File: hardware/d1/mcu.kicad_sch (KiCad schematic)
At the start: 3 parts, among them U2 STM32G0B1VCT6, U3 STM32G0B1KBU6N, X1 X322516MLB4SI

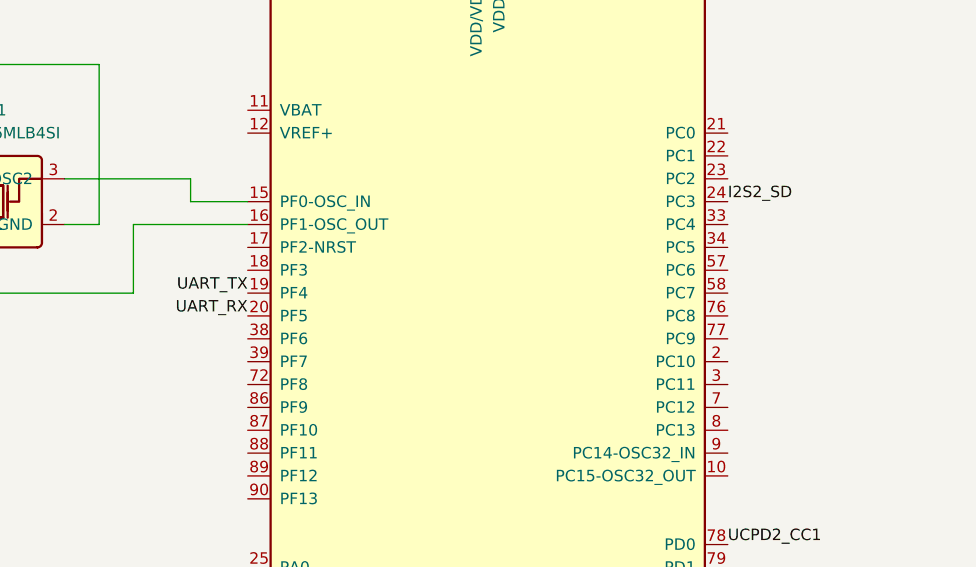
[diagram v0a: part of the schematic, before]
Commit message: Change uart pins, add components
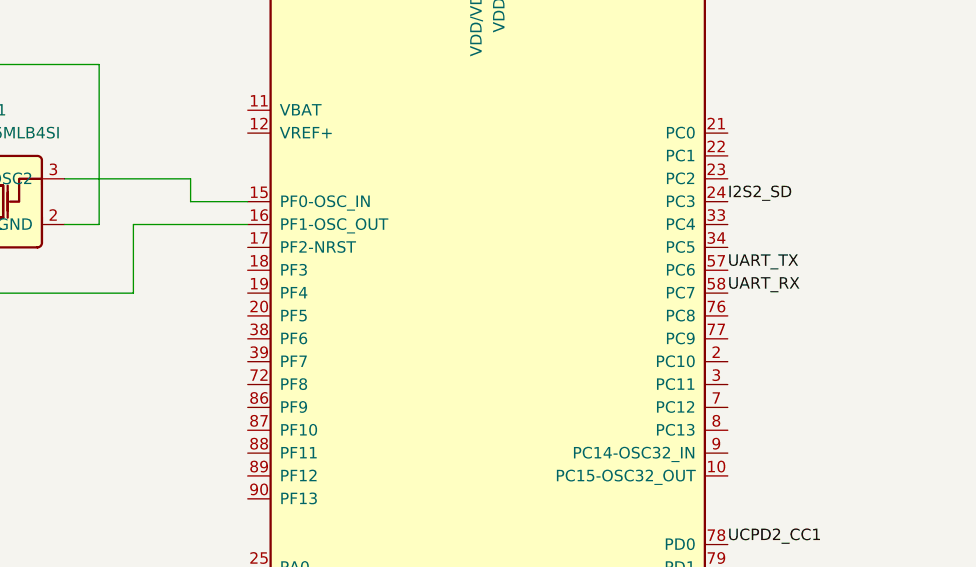
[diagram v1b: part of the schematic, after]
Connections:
- net UART_RX: now also U2.58 (PC7); no longer U2.20 (PF5)
- net UART_TX: now also U2.57 (PC6); no longer U2.19 (PF4)
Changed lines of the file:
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@@
-		)
-	)
-	(label "UART_TX"
-		(at 83.82 58.42 180)
-		(effects
-			(font
-				(size 1.27 1.27)
-			)
-			(justify right bottom)
 		)
 	)
@@
 		)
 	)
+	(label "UART_RX"
+		(at 137.16 58.42 0)
+		(effects
+			(font
+				(size 1.27 1.27)
+			)
+			(justify left bottom)
+		)
+	)
 	(label "USB_DP"
 		(at 83.82 119.38 180)
@@
 		)
 	)
-	(label "UART_RX"
-		(at 83.82 60.96 180)
-		(effects
-			(font
-				(size 1.27 1.27)
-			)
-			(justify right bottom)
-		)
-	)
 	(label "SWDIO"
 		(at 83.82 121.92 180)
@@
 		)
 	)
+	(label "UART_TX"
+		(at 137.16 55.88 0)
+		(effects
+			(font
+				(size 1.27 1.27)
+			)
+			(justify left bottom)
+		)
+	)

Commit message: Add new parts
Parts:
- added C18: 1uF 25V X5R, JLCImport:CL05A105KA5NQNC, symbol JLCImport:CL05A105KA5NQNC
- added C20: 100nF 16V X7R, JLCImport:CL05B104KO5NNNC, symbol JLCImport:CL05B104KO5NNNC
- added L4: BLM15AG601SN1D, JLCImport:BLM15AG601SN1D, symbol JLCImport:BLM15AG601SN1D
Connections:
- net GND: now also U2.14 (VSS/VSSA), U2.63 (VSS), C18.2, C20.2; no longer X1.2 (GND), X1.4 (GND)
- net at U2.12 (VREF+): now also C18.1, C20.1, L4.2
- new net: X1.2 (GND), X1.4 (GND)
- new net +1V8_D: L4.1

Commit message: Pre-finalize sch
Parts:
- removed X1: X322516MLB4SI, JLCImport:X322516MLB4SI, symbol JLCImport:X322516MLB4SI
- added C49: 10nF 50V X7R, Capacitor_SMD:C_0402_1005Metric, symbol JLCImport:CL05B103KB5NNNC
- added C50, C52, C54, C56: 100nF 16V X7R, JLCImport:CL05B104KO5NNNC, symbol JLCImport:CL05B104KO5NNNC
- added C53, C55: 4.7uF 10V X5R, JLCImport:CL05A475MP5NRNC, symbol JLCImport:CL05A475MP5NRNC
- added R11, R12: 2.2kΩ, Resistor_SMD:R_0402_1005Metric, symbol JLCImport:0402WGF2201TCE
- added R14, R15: 100kΩ, JLCImport:0402WGF1003TCE, symbol JLCImport:0402WGF1003TCE
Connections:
- net +1V8_D: now also U2.11 (VBAT), U2.13 (VDD/VDDA), C50.1, C52.1, C53.1, R11.1, R12.1
- net GND: now also C49.1, C50.2, C52.2, C53.2, C54.2, C55.2, C56.2, R15.1
- net I2C2_SCL: now also U2.98 (PB6), R11.2; no longer U2.56 (PA9)
- net I2C2_SDA: now also U2.99 (PB7), R12.2; no longer U2.69 (PA10)
- net +3V3_D: now reaches U3.20 (PC6)
- net +3V3_D: now also U2.64 (VDDIO2), C54.1, C55.1
- net at U2.17 (PF2-NRST): now also C56.1
- net ADC1_IN1: now reaches U2.25 (PA0)
- net ADC1_IN2: now reaches U2.26 (PA1)
- net ADC1_IN3: now reaches U2.27 (PA2)
- net ADC1_IN4: now reaches U2.28 (PA3)
- net ADC1_IN5: now reaches U2.29 (PA4)
- net ADC1_IN5: now also C49.2, R14.1, R15.2
- new net JACK_SLEEVE: R14.2
- no-connect marks 0 -> 4
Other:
- note added: "For headset buttons decoding"

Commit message: Fix issue, add exti
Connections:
- net GPIO_EXTI1: now also U2.95 (PE1)
- net GPIO_EXTI2: now also U2.96 (PE2)
- net GPIO_EXTI3: now also U2.97 (PE3)
- net GPIO_EXTI0: now reaches U2.94 (PE0)
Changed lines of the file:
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@@
+		)
+	)
+	(label "GPIO_EXTI2"
+		(at 137.16 137.16 0)
+		(effects
+			(font
+				(size 1.27 1.27)
+			)
+			(justify left bottom)
 		)
 	)
@@
 		)
 	)
+	(label "GPIO_EXTI0"
+		(at 137.16 132.08 0)
+		(effects
+			(font
+				(size 1.27 1.27)
+			)
+			(justify left bottom)
+		)
+	)
 	(label "ADC1_IN2"
 		(at 39.37 167.64 0)
@@
 		)
 	)
+	(label "GPIO_EXTI1"
+		(at 137.16 134.62 0)
+		(effects
+			(font
+				(size 1.27 1.27)
+			)
+			(justify left bottom)
+		)
+	)
 	(label "ADC1_IN1"
 		(at 77.47 88.9 180)
@@
 		(effects
 			(font
+				(size 1.27 1.27)
+			)
+			(justify left bottom)
+		)
+	)
+	(label "GPIO_EXTI3"
+		(at 137.16 139.7 0)
+		(effects
+			(font

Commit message: Fixes
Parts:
- added R31, R32, R33, R34: 100kΩ, JLCImport:0402WGF1003TCE, symbol JLCImport:0402WGF1003TCE
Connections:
- net ADC1_IN5 is gone; now on net ADC1_IN4: C49.2, R14.1, R15.2, U2.29 (PA4)
- net I2C2_SCL is gone; now on net I2C1_SCL: R11.2, U2.98 (PB6)
- net I2C2_SDA is gone; now on net I2C1_SDA: R12.2, U2.99 (PB7)
- net ADC1_IN1: now also U2.26 (PA1); no longer U2.25 (PA0)
- net ADC1_IN2: now also U2.27 (PA2); no longer U2.26 (PA1)
- net ADC1_IN3: now also U2.28 (PA3); no longer U2.27 (PA2)
- net ADC1_IN4: no longer U2.28 (PA3)
- net CLOCK_EN_22_5792: now also U2.84 (PD6)
- net CLOCK_EN_24_576: now also U2.83 (PD5)
- net GND: now also R31.1, R32.1, R33.1, R34.1
- net UCPD1_DBCC1: now reaches U2.56 (PA9)
- net UCPD1_DBCC1: now also R31.2
- net UCPD1_DBCC2: now reaches U2.69 (PA10)
- net UCPD1_DBCC2: now also R32.2
- net UCPD2_DBCC1: now reaches U2.79 (PD1)
- net UCPD2_DBCC1: now also R33.2
- net UCPD2_DBCC2: now reaches U2.81 (PD3)
- net UCPD2_DBCC2: now also R34.2
- net CS_RESET/: now reaches U2.85 (PD7)
- new net ADC1_IN0: U2.25 (PA0)

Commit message: Pre power change
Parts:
- removed U3: STM32G0B1KBU6N, JLCImport:STM32G0B1KBU6N, symbol JLCImport:STM32G0B1KBU6N
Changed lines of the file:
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@@
-		)
-	)
-	(label "VDDIO2"
-		(at 181.61 83.82 180)
-		(effects
-			(font
-				(size 1.27 1.27)
-			)
-			(justify right bottom)
 		)
 	)
@@
 					(unit 1)
 				)
-			)
-		)
-	)
-	(symbol
-		(lib_id "JLCImport:STM32G0B1KBU6N")
-		(at 207.01 97.79 0)
-		(unit 1)
-		(body_style 1)
-		(exclude_from_sim yes)
-		(in_bom no)
-		(on_board no)
-		(in_pos_files no)
-		(dnp yes)
-		(fields_autoplaced yes)
-		(property "Reference" "U3"
-			(at 207.01 62.23 0)
-			(show_name no)
-			(do_not_autoplace no)
-			(effects
-				(font
-					(size 1.27 1.27)
-				)
-			)
-		)
-		(property "Value" "STM32G0B1KBU6N"
-			(at 207.01 64.77 0)
-			(show_name no)
-			(do_not_autoplace no)
-			(effects
-				(font
-					(size 1.27 1.27)
-				)
-			)
-		)
-		(property "Footprint" "JLCImport:STM32G0B1KBU6N"
-			(at 207.01 97.79 0)
-			(hide yes)
-			(show_name no)
-			(do_not_autoplace no)
-			(effects
-				(font
-					(size 1.27 1.27)
-				)
-			)
-		)
-		(property "Datasheet" "https://item.szlcsc.com/692132.html"
-			(at 207.01 97.79 0)
-			(hide yes)
-			(show_name no)
-			(do_not_autoplace no)
-			(effects
-				(font
-					(size 1.27 1.27)
-				)
-			)
-		)
-		(property "Description" "UFQFPN-32(5x5) Microcontrollers (MCU/MPU/SOC) ROHS"
-			(at 207.01 97.79 0)
-			(hide yes)
-			(show_name no)
-			(do_not_autoplace no)
-			(effects
-				(font
-					(size 1.27 1.27)
-				)
-			)
-		)
-		(property "LCSC" "C5270168"
-			(at 207.01 97.79 0)
-			(hide yes)
-			(show_name no)
-			(do_not_autoplace no)
-			(effects
-				(font
-					(size 1.27 1.27)
-				)
-			)
-		)
-		(property "Manufacturer" "STMicroelectronics"
-			(at 207.01 97.79 0)
-			(hide yes)
-			(show_name no)
-			(do_not_autoplace no)
-			(effects
-				(font
-					(size 1.27 1.27)
-				)
-			)
-		)
-		(property "Manufacturer Part" "STM32G0B1KBU6N"
-			(at 207.01 97.79 0)
-			(hide yes)
-			(show_name no)
-			(do_not_autoplace no)
-			(effects
-				(font
-					(size 1.27 1.27)
-				)
-			)
-		)
-		(pin "20"
-		)
-		(pin "19"
-		)
-		(pin "22"
-		)
-		(pin "21"
-		)
-		(pin "18"
-		)
-		(pin "17"
-		)
-		(pin "30"
-		)
-		(pin "29"
-		)
-		(pin "28"
-		)
-		(pin "27"
-		)
-		(pin "26"
-		)
-		(pin "25"
-		)
-		(pin "24"
-		)
-		(pin "23"
-		)
-		(pin "11"
-		)
-		(pin "15"
-		)
-		(pin "16"
-		)
-		(pin "8"
-		)
-		(pin "14"
-		)
-		(pin "13"
-		)
-		(pin "9"
-		)
-		(pin "1"
-		)
-		(pin "2"
-		)
-		(pin "12"
-		)
-		(pin "6"
-		)
-		(pin "10"
-		)
-		(pin "3"
-		)
-		(pin "4"
-		)
-		(pin "7"
-		)
-		(pin "5"
-		)
-		(pin "33"
-		)
-		(pin "32"
-		)
-		(pin "31"
-		)
-		(instances
-			(project "DrunkEarPhoneAdapter"
-				(path "/df940915-8af0-46f9-b18a-23d4684ae671/c6b936ac-23e1-4f20-8d3d-ded05833abcb"
-					(reference "U3")
-					(unit 1)
-				)

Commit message: Fixes
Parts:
- added J3: SWD, JLCImport:Conn_1x5_1.27, symbol Connector_Generic:Conn_01x05
- added J4: UART, JLCImport:Conn_1x5_1.27, symbol Connector_Generic:Conn_01x05
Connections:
- net +3V3_D: now also C50.1, C53.1, L4.1, R11.1, R12.1, U2.13 (VDD/VDDA), J3.1 (Pin_1), J4.1 (Pin_1)
- net GND: now also C56.1, J3.5 (Pin_5), J4.5 (Pin_5); no longer C56.2
- net SWCLK: now also J3.3 (Pin_3)
- net SWDIO: now also J3.2 (Pin_2)
- net UART_RX: now also J4.2 (Pin_2)
- net UART_TX: now also J4.3 (Pin_3)
- net NRST: now reaches U2.17 (PF2-NRST)
- net NRST: now also C56.2, J3.4 (Pin_4); no longer C56.1
- net at C18.1, C20.1, L4.2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: now also C52.1, U2.11 (VBAT)
- net PHONE_EN: now reaches U2.86 (PF9)
- removed net +1V8_D: C50.1, C52.1, C53.1, L4.1, R11.1, R12.1, U2.11 (VBAT), U2.13 (VDD/VDDA)
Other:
- moved on the sheet: C52, C56

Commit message: Fixesss
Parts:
- added C69: 100nF 16V X7R, JLCImport:CL05B104KO5NNNC, symbol JLCImport:CL05B104KO5NNNC
- added Q3: DMG1012T-7, Package_TO_SOT_SMD:SOT-523, symbol JLCImport:DMG1012T-7
- added R39: 100kΩ, JLCImport:0402WGF1003TCE, symbol JLCImport:0402WGF1003TCE
- J3, J4: now left out of the parts list
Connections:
- net +3V3_D: now also U2.11 (VBAT), C69.1
- net GND: now also C69.2, Q3.2 (S), R39.1
- net UCPD1_CC1: now also Q3.3 (D)
- net at C18.1, C20.1, C52.1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: no longer U2.11 (VBAT)
- net UCPD2_FRSTX1: now reaches U2.51 (PB12)
- net UCPD1_FRSTX2: now reaches U2.53 (PB14)
- net UCPD1_FRSTX1: now reaches U2.7 (PC12)
- net UCPD1_FRSTX1: now also Q3.1 (G), R39.2
- net UCPD2_FRSTX2: now reaches U2.76 (PC8)
